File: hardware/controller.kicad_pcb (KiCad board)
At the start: 4 copper layers, 32 x 93.3 mm, 37 parts, among them J1 Connector, USB-TYPE-C-16P, U1 ESP32-C6-WROOM-1, U3 TPS62840YBGR

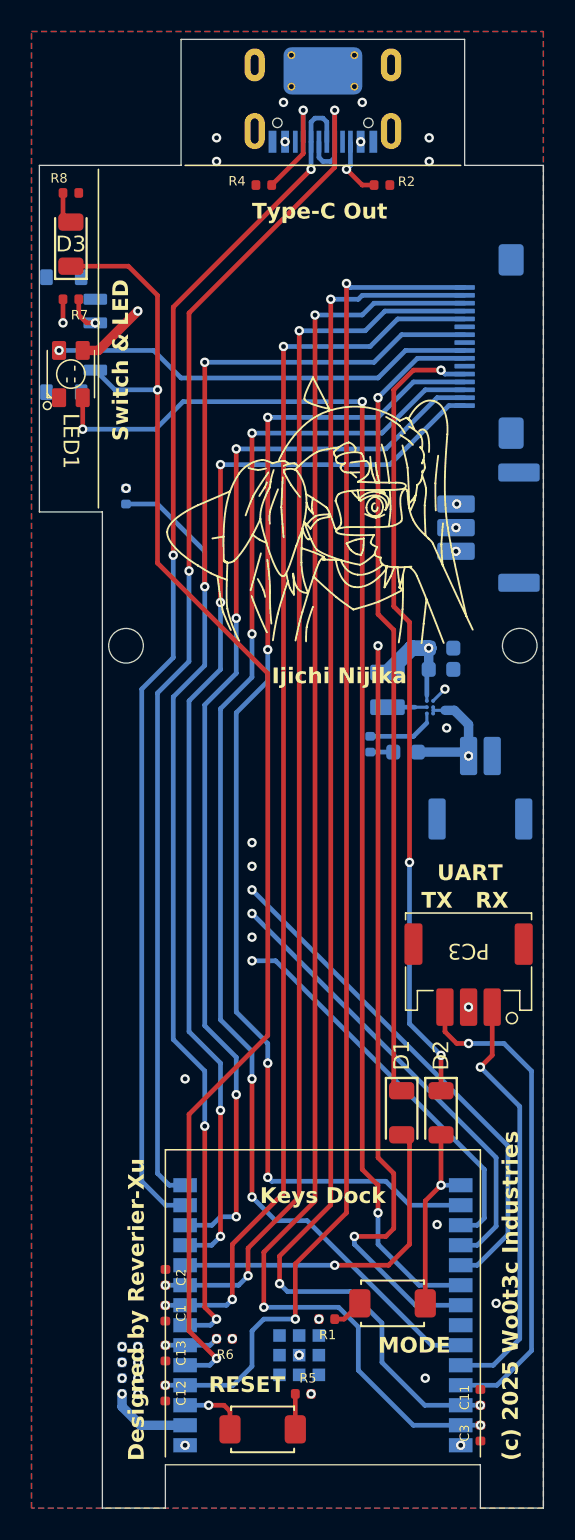
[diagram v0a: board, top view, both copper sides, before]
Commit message: :sparkles: add CH334P & CH343P to components library
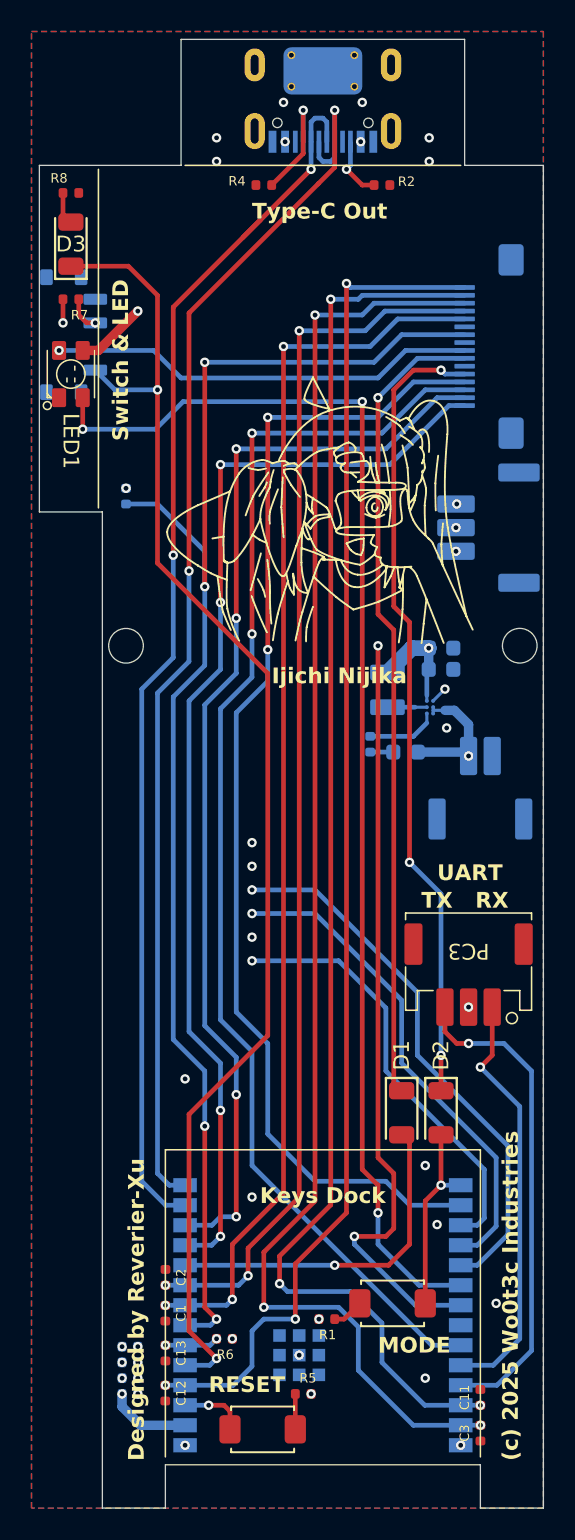
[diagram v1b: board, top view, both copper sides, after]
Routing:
- net /EINK_DC: track 32.4 -> 34.8 mm
- net /EINK_SPI_MOSI: track 29.0 -> 31.4 mm
- net /EINK_SPI_CLK: track 25.0 -> 27.4 mm
- net /KEYS_CH_D: track 76.3 -> 74.7 mm, vias 4 -> 2
- net /USB_D-: track 77.5 -> 79.1 mm
- net /KEYS_CH_C: track 81.9 -> 80.8 mm, vias 4 -> 2
- net P,E: vias 20 -> 22
